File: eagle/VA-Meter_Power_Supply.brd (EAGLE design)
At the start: 100 x 80 mm, 18 parts, among them IC2 7805TV, T1 2SA1359

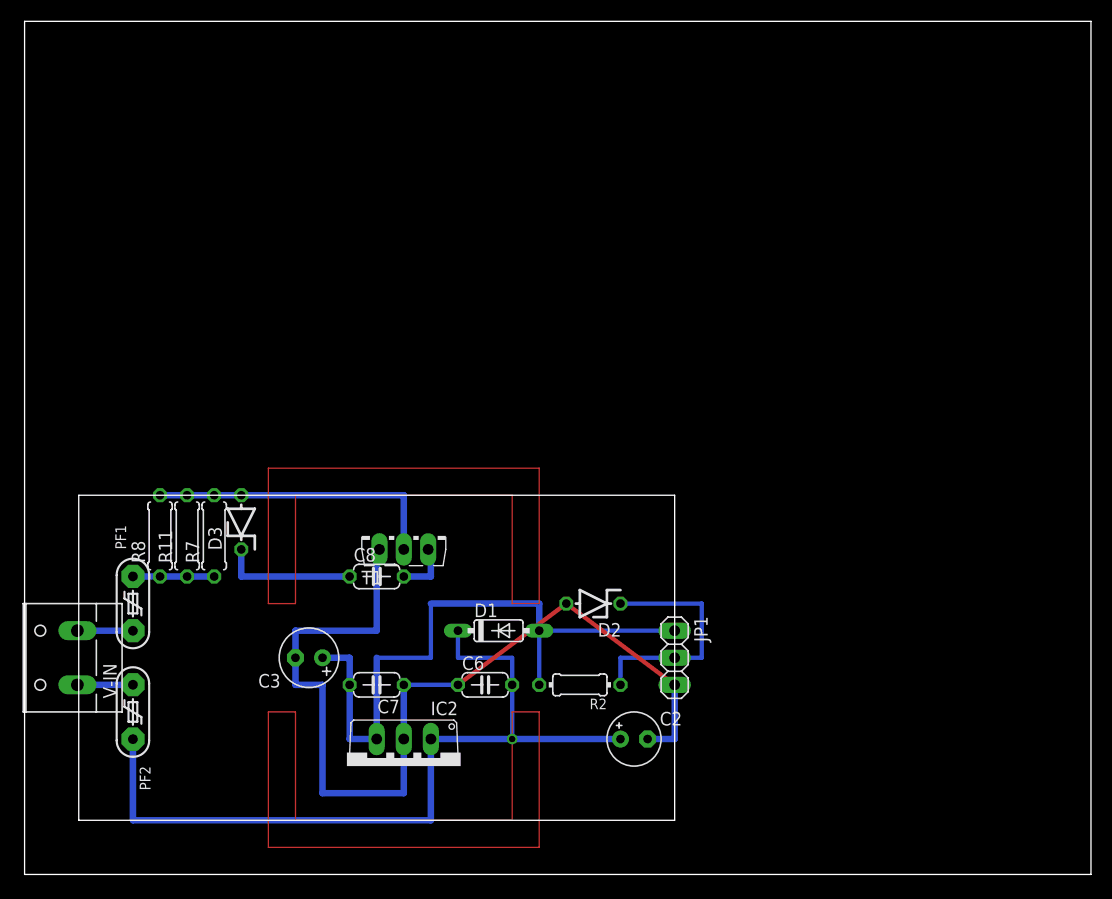
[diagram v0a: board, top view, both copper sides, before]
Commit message: Power Supply 回路図、基板図修正
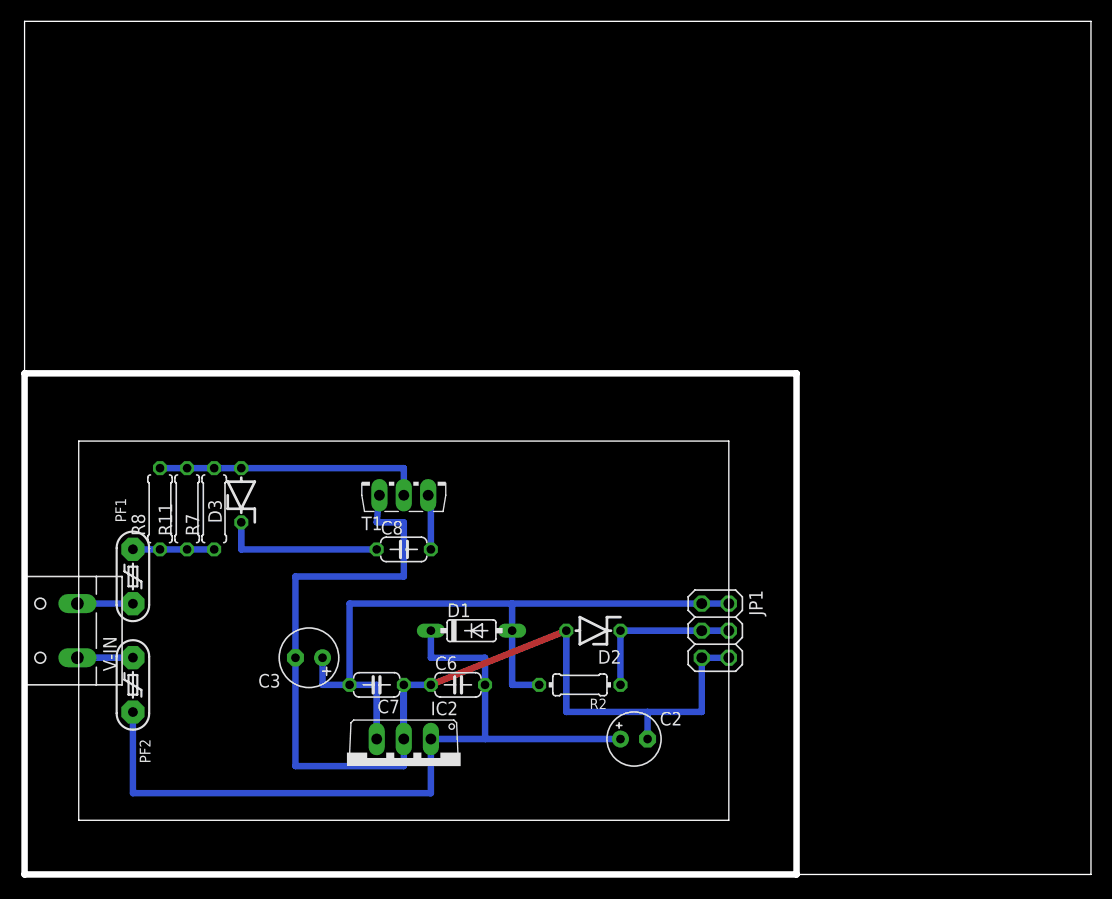
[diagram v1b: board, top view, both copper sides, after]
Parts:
- JP1: device pinhead:1X03 -> pinhead:2X03
- moved T1 5.08 mm to (35.6, 36.8)
- moved JP1 4.58 mm to (64.8, 22.9)
- moved C8 3.59 mm to (35.6, 30.5)
- moved D1 2.54 mm to (41.9, 22.9)
- moved PF1 2.54 mm to (10.2, 27.9)
- moved PF2 2.54 mm to (10.2, 17.8)
- moved C6 2.54 mm to (40.6, 17.8)
- moved D2 2.54 mm to (53.3, 22.9)
- moved D3 2.54 mm to (20.3, 35.6)
- moved R11 2.54 mm to (15.2, 34.3)
- moved R7 2.54 mm to (17.8, 34.3)
- moved R8 2.54 mm to (12.7, 34.3)
- moved V-IN 2.54 mm to (4.32, 22.9)
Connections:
- net 3.3V: now also JP1.3, JP1.4; no longer JP1.2
- net 5V: now also JP1.2
- net V-GND: now also JP1.5, JP1.6; no longer JP1.3
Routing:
- net N$2: track 96.5 -> 0.00 mm
- net N$3: track 96.5 -> 0.00 mm
- net V-GND: track 89.2 -> 107.7 mm
- net 3.3V: track 22.9 -> 15.2 mm
- net 5V: track 61.0 -> 66.0 mm
- net N$1: track 27.9 -> 25.4 mm
- net GND: track 12.7 -> 15.2 mm
- net +15V: track 76.2 -> 73.7 mm, vias 1 -> 0
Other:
- outline, holes or cut-outs redrawn

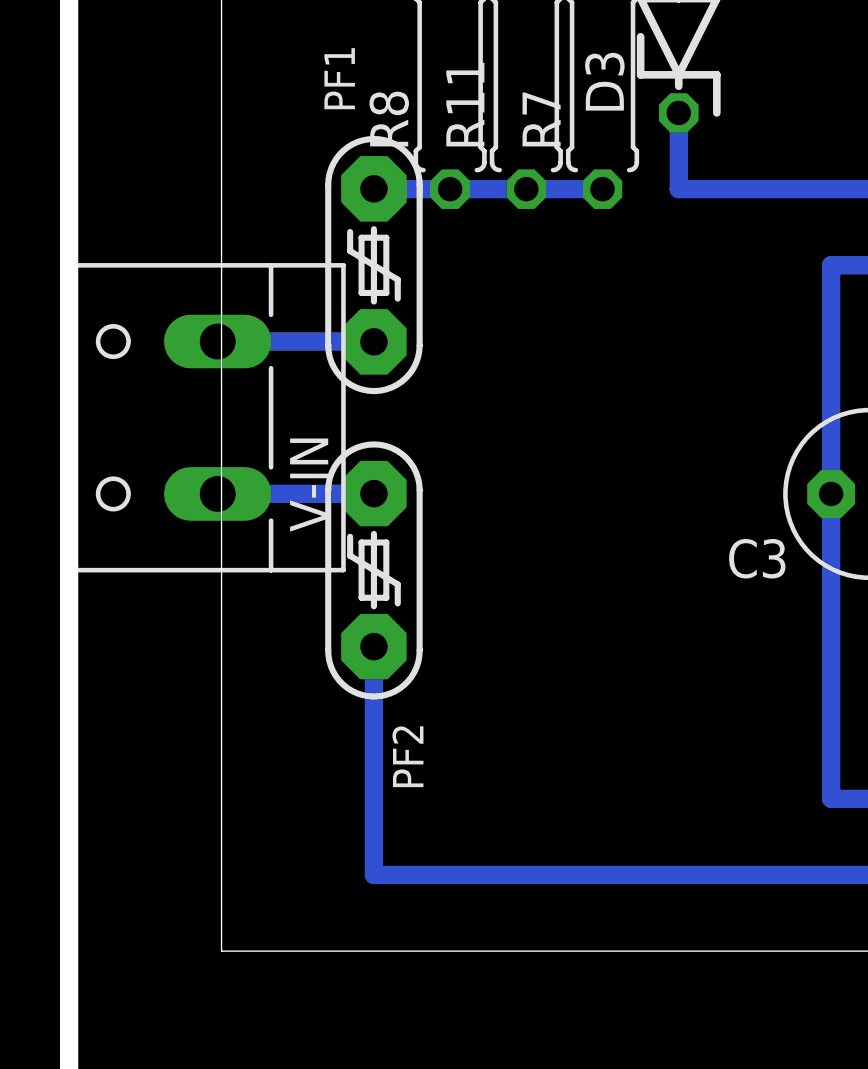
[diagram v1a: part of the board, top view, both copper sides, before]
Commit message: VA-Meter_Power_Supply 測定部電源の回路図、基板図修正 入力端子にGNDを追加
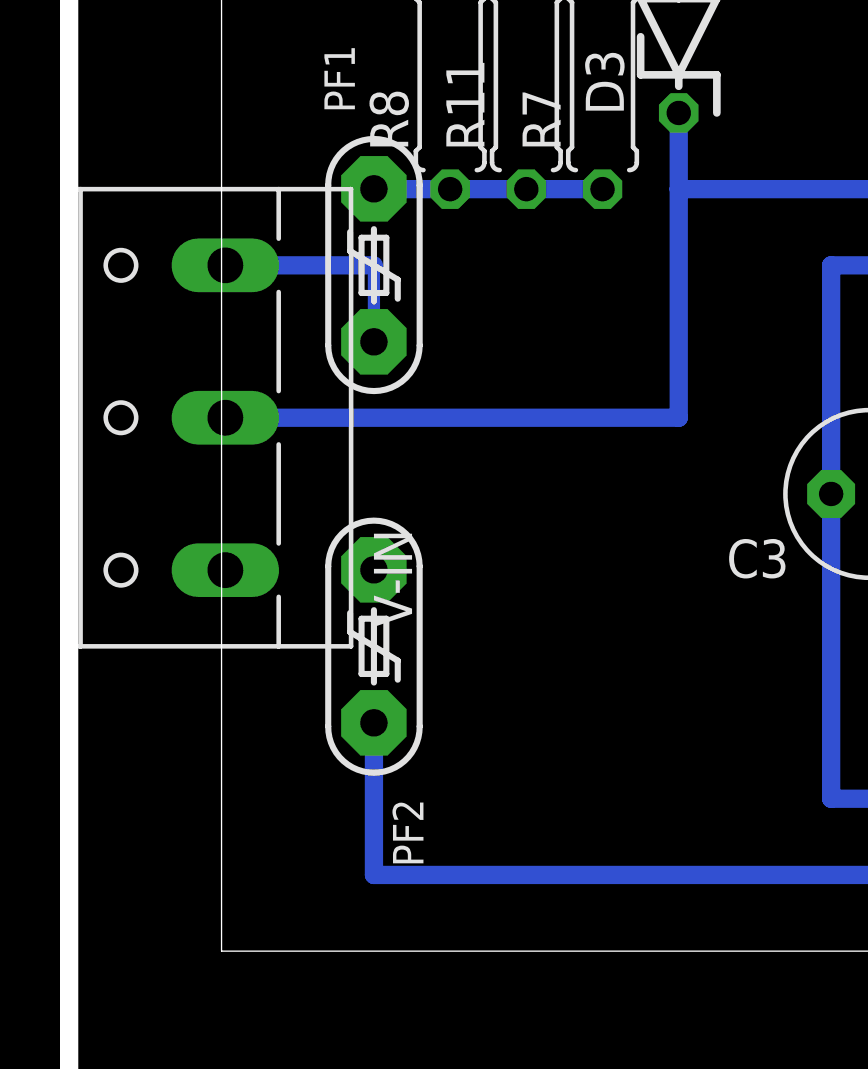
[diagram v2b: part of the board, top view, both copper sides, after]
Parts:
- V-IN: device con-wago-508:W237-132 -> con-wago-508:W237-133
- moved PF2 2.54 mm to (10.2, 15.2)
- moved V-IN 0.25 mm to (4.57, 22.9)
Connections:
- net GND: now also V-IN.2
- net N$7: now also V-IN.3; no longer V-IN.2
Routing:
- net GND: track 15.2 -> 38.0 mm
- net N$6: track 5.21 -> 0.00 mm
- net +15V: track 73.7 -> 71.1 mm
- net N$7: track 5.21 -> 7.50 mm
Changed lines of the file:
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@@
 <setting verticaltext="up"/>
 </settings>
-<grid distance="0.1" unitdist="inch" unit="mm" style="dots" multiple="1" display="yes" altdistance="1.27" altunitdist="mm" altunit="mm"/>
+<grid distance="0.1" unitdist="inch" unit="mm" style="dots" multiple="1" display="yes" altdistance="0.254" altunitdist="mm" altunit="mm"/>
 <layers>
 <layer number="1" name="Top" color="4" fill="1" visible="yes" active="yes"/>
@@
 <layer number="98" name="Guide" color="6" fill="1" visible="no" active="no"/>
 <layer number="99" name="SpiceOrder" color="5" fill="1" visible="no" active="no"/>
-<layer number="100" name="Mesh" color="7" fill="1" visible="yes" active="yes"/>
+<layer number="100" name="Mesh" color="7" fill="1" visible="no" active="yes"/>
 </layers>
 <board>
@@
 <element name="C2" library="rcl" package="E2,5-5" value="10u" x="57.15" y="12.7"/>
 <element name="C3" library="rcl" package="E2,5-6" value="100u" x="26.67" y="20.32" rot="R180"/>
-<element name="V-IN" library="con-wago-508" package="W237-132" value="" x="4.318" y="22.86" rot="R90">
-<attribute name="OC_NEWARK" value="unknown" x="9.398" y="41.91" size="1.778" layer="27" rot="R90" display="off"/>
-<attribute name="MPN" value="" x="9.398" y="41.91" size="1.778" layer="27" rot="R90" display="off"/>
-<attribute name="MF" value="" x="9.398" y="41.91" size="1.778" layer="27" rot="R90" display="off"/>
-<attribute name="OC_FARNELL" value="unknown" x="9.398" y="41.91" size="1.778" layer="27" rot="R90" display="off"/>
-</element>
 <element name="D1" library="diode" package="DO35-7" value="1S2" x="41.91" y="22.86"/>
 <element name="D2" library="diode" package="ZDIO-5" value="3.6V" x="53.34" y="22.86" rot="R180"/>
@@
 <element name="R7" library="rcl" package="0207/7" value="1.5k" x="17.78" y="34.29" rot="R90"/>
 <element name="R11" library="rcl" package="0207/7" value="1.5k" x="15.24" y="34.29" rot="R90"/>
-<element name="PF2" library="polyswitch" package="PF-5.1" value="PTC-PF-5.1" x="10.16" y="17.78" rot="R270"/>
+<element name="PF2" library="polyswitch" package="PF-5.1" value="PTC-PF-5.1" x="10.16" y="15.24" rot="R270"/>
 <element name="PF1" library="polyswitch" package="PF-5.1" value="PTC-PF-5.1" x="10.16" y="27.94" rot="R90"/>
 <element name="JP1" library="pinhead" package="2X03" value="" x="64.77" y="22.86" rot="R270"/>
+<element name="V-IN" library="con-wago-508" package="W237-133" value="" x="4.572" y="22.86" rot="R90">
+<attribute name="OC_NEWARK" value="unknown" x="4.572" y="22.86" size="1.778" layer="27" rot="R90" display="off"/>
+<attribute name="MPN" value="" x="4.572" y="22.86" size="1.778" layer="27" rot="R90" display="off"/>
+<attribute name="MF" value="" x="4.572" y="22.86" size="1.778" layer="27" rot="R90" display="off"/>
+<attribute name="OC_FARNELL" value="unknown" x="4.572" y="22.86" size="1.778" layer="27" rot="R90" display="off"/>
+</element>
 </elements>
 <signals>
@@
 <wire x1="20.32" y1="33.02" x2="20.32" y2="30.48" width="0.6096" layer="16"/>
 <wire x1="20.32" y1="30.48" x2="33.02" y2="30.48" width="0.6096" layer="16"/>
+<contactref element="V-IN" pad="2"/>
+<wire x1="5.207" y1="22.86" x2="20.32" y2="22.86" width="0.6096" layer="16"/>
+<wire x1="20.32" y1="22.86" x2="20.32" y2="30.48" width="0.6096" layer="16"/>
 </signal>
 <signal name="+15V">
@@
 <contactref element="C6" pad="2"/>
 <contactref element="PF2" pad="2"/>
-<wire x1="10.16" y1="15.23" x2="10.16" y2="7.62" width="0.6096" layer="16"/>
+<wire x1="10.16" y1="12.69" x2="10.16" y2="7.62" width="0.6096" layer="16"/>
 <wire x1="10.16" y1="7.62" x2="38.1" y2="7.62" width="0.6096" layer="16"/>
 <wire x1="38.1" y1="7.62" x2="38.1" y2="12.7" width="0.6096" layer="16"/>
@@
 </signal>
 <signal name="N$6">
+<contactref element="PF2" pad="1"/>
 <contactref element="V-IN" pad="1"/>
-<contactref element="PF2" pad="1"/>
-<wire x1="4.953" y1="20.32" x2="10.16" y2="20.33" width="0.6096" layer="16"/>
+<wire x1="5.207" y1="17.78" x2="10.16" y2="17.79" width="0" layer="19" extent="1-1"/>
 </signal>
 <signal name="N$7">
-<contactref element="V-IN" pad="2"/>
 <contactref element="PF1" pad="1"/>
-<wire x1="4.953" y1="25.4" x2="10.16" y2="25.4" width="0.6096" layer="16"/>
-<wire x1="10.16" y1="25.4" x2="10.16" y2="25.39" width="0" layer="19" extent="1-16"/>
+<contactref element="V-IN" pad="3"/>
+<wire x1="5.207" y1="27.94" x2="10.16" y2="27.94" width="0.6096" layer="16"/>
+<wire x1="10.16" y1="27.94" x2="10.16" y2="25.39" width="0.4064" layer="16"/>
 </signal>
 <signal name="5V">
